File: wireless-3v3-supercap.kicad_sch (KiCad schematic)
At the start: 3 parts, among them J1 POWER-OUT, J2 POWER-IN

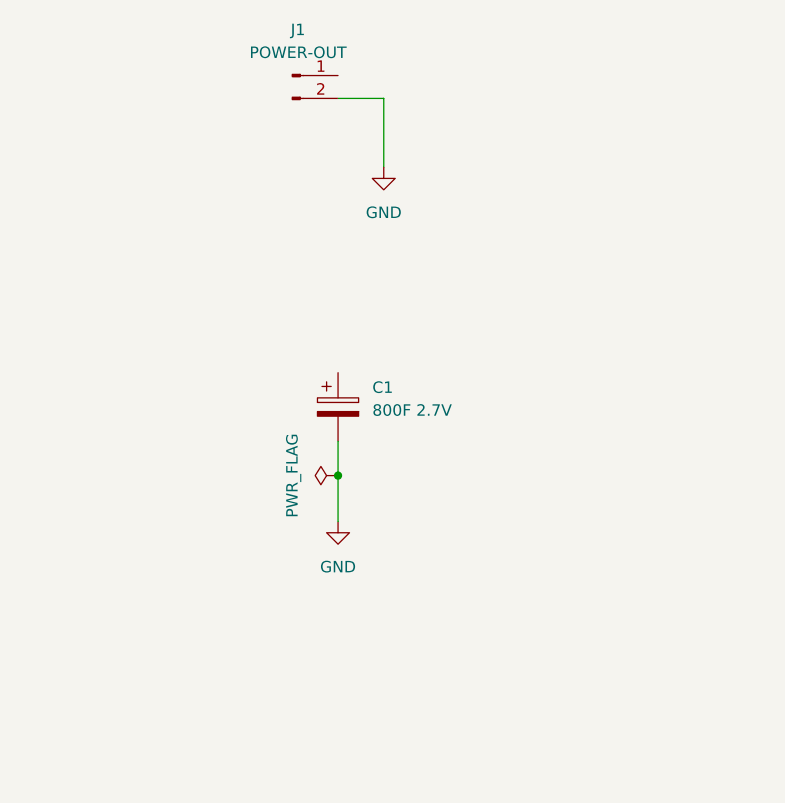
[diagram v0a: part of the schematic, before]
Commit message: Add a discharge switch
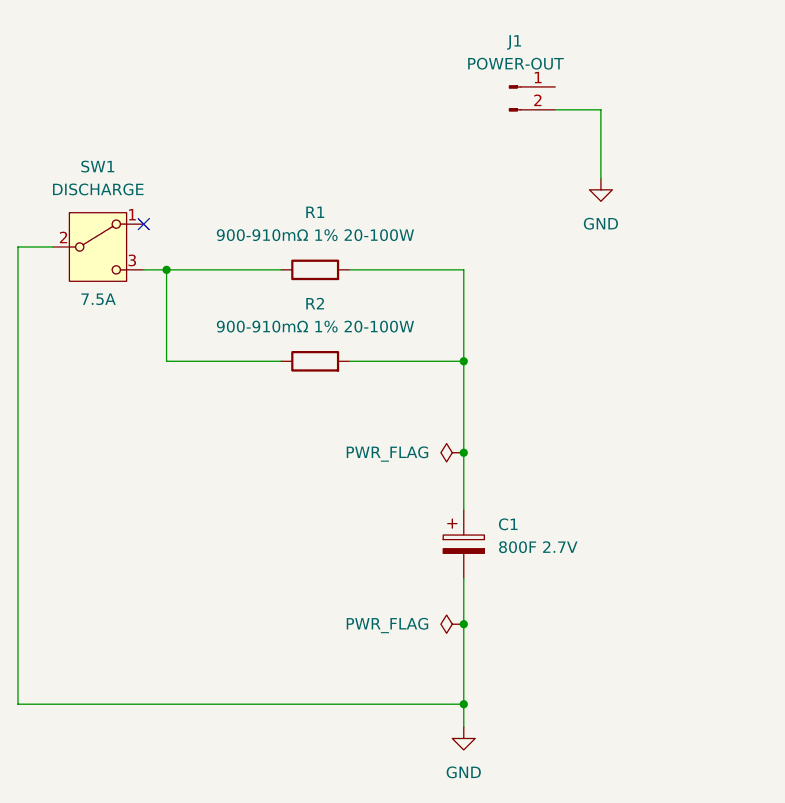
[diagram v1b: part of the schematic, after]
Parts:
- added R1, R2: 900-910mΩ 1% 20-100W, Package_TO_SOT_THT:TO-247-2_Horizontal_TabDown, symbol Device:R
- added SW1: DISCHARGE, symbol Switch:SW_SPDT
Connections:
- net GND: now also SW1.2 (B)
- net at C1.1: now also R1.2, R2.2
- new net: R1.1, R2.1, SW1.3 (C)
- no-connect marks 0 -> 1
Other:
- moved on the sheet: C1, J1

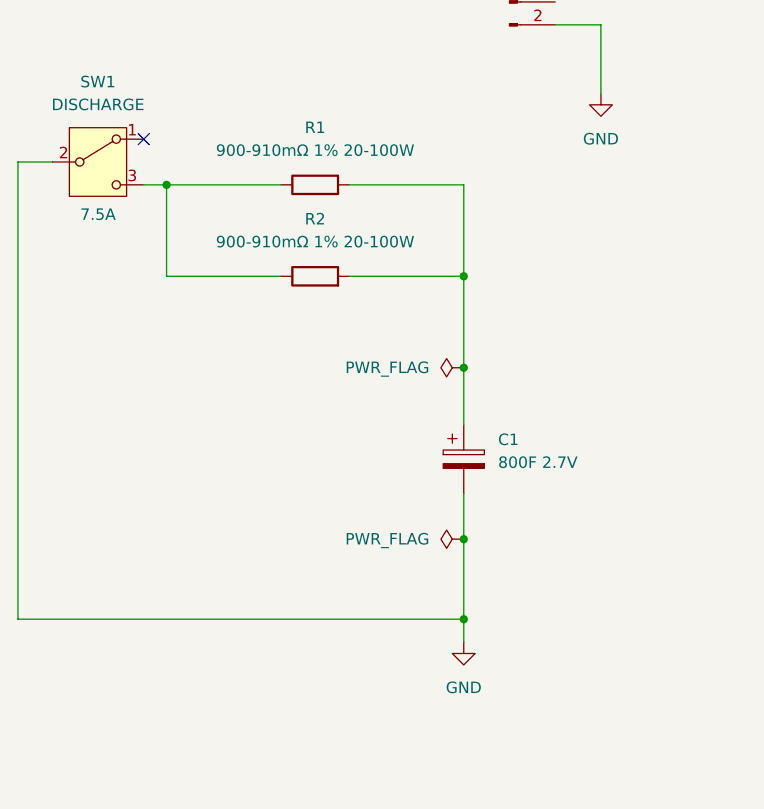
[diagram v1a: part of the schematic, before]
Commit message: Add heatsinks to the discharge resistors
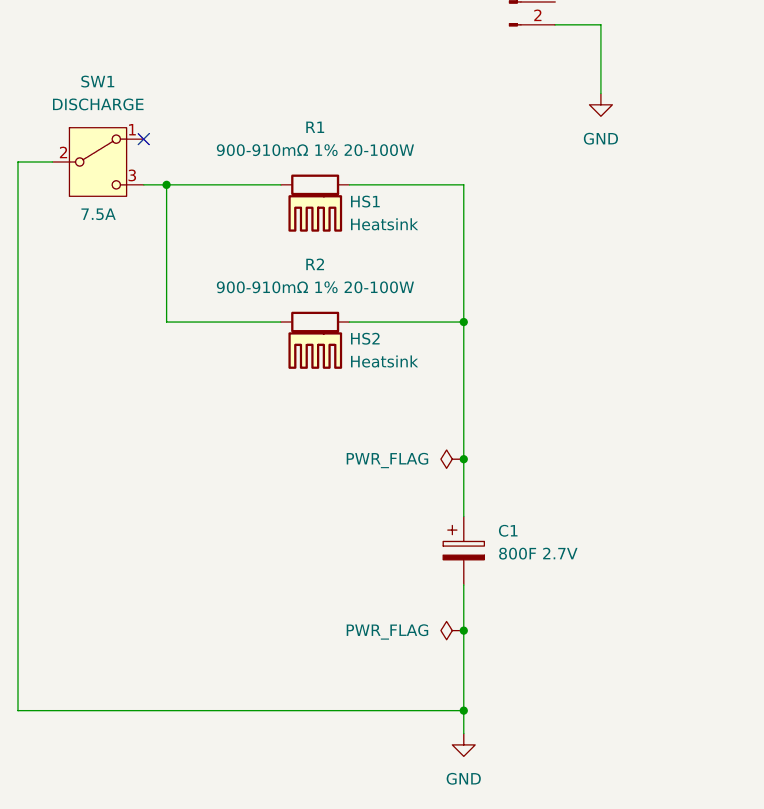
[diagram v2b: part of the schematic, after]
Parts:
- added HS1, HS2: Heatsink, symbol Mechanical:Heatsink
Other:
- moved on the sheet: C1, R2

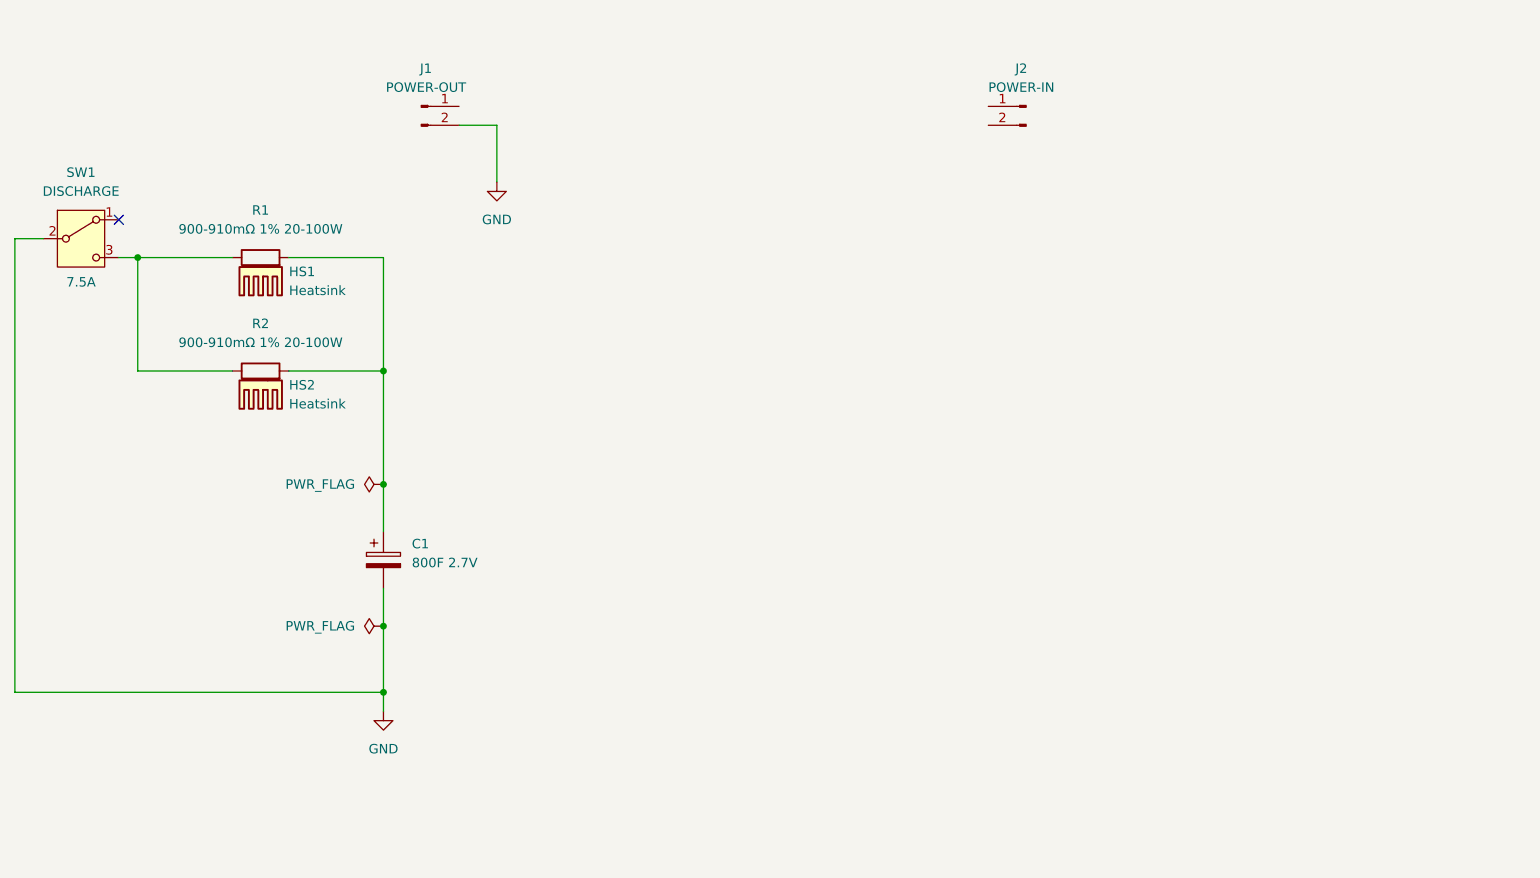
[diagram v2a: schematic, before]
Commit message: Add BQ33100PWR
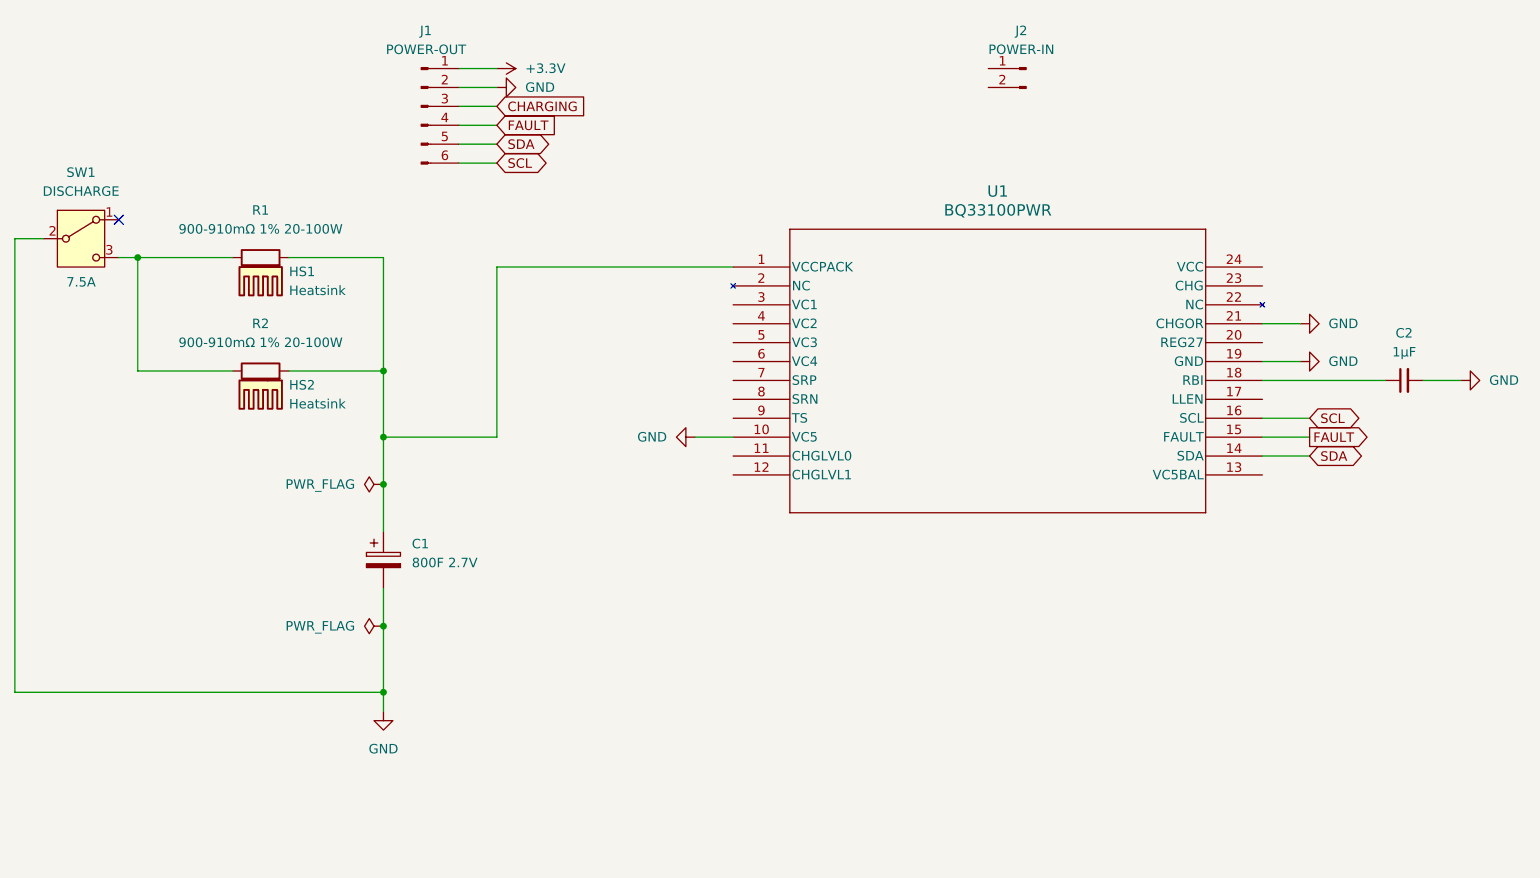
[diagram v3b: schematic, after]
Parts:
- added C2: 1µF, symbol Device:C_Small
- added U1: BQ33100PWR, PW24, symbol BQ33100PWR:BQ33100PWR
- J1: footprint Connector_PinHeader_2.54mm:PinHeader_1x02_P2.54mm_Vertical -> Connector_PinHeader_2.54mm:PinHeader_1x06_P2.54mm_Vertical; symbol Connector:Conn_01x02_Pin -> Connector:Conn_01x06_Pin
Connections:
- net GND: now also C2.2, U1.10 (VC5), U1.19 (GND), U1.21 (CHGOR)
- net +3.3V: now reaches J1.1 (Pin_1)
- net at C1.1, R1.2, R2.2: now also U1.1 (VCCPACK)
- new net: C2.1, U1.18 (RBI)
- new net CHARGING: J1.3 (Pin_3)
- new net FAULT: J1.4 (Pin_4), U1.15 (FAULT)
- new net SCL: J1.6 (Pin_6), U1.16 (SCL)
- new net SDA: J1.5 (Pin_5), U1.14 (SDA)
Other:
- moved on the sheet: J2

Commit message: Remove BQ33100PWR and discharge resistors
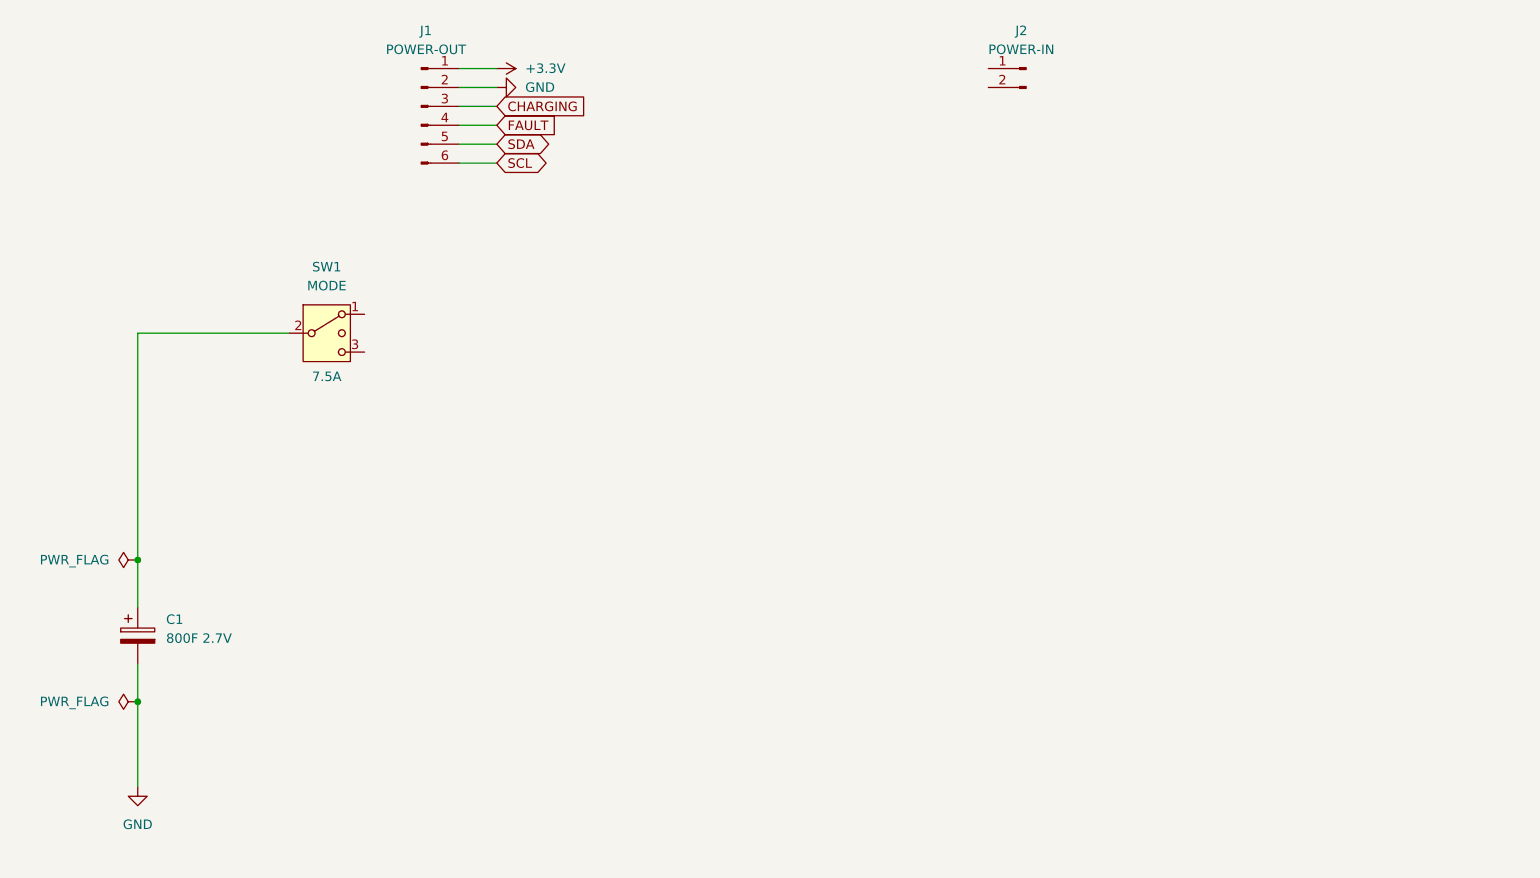
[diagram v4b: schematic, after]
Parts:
- removed C2: 1µF, symbol Device:C_Small
- removed HS1, HS2: Heatsink, symbol Mechanical:Heatsink
- removed R1, R2: 900-910mΩ 1% 20-100W, Package_TO_SOT_THT:TO-247-2_Horizontal_TabDown, symbol Device:R
- removed U1: BQ33100PWR, PW24, symbol BQ33100PWR:BQ33100PWR
- SW1: value DISCHARGE -> MODE; symbol Switch:SW_SPDT -> Switch:SW_SPDT_MSM
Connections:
- net GND: no longer SW1.2 (B)
- net at C1.1: now also SW1.2 (3)
- no-connect marks 1 -> 0
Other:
- moved on the sheet: C1

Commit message: Add discharge circuit, and main component for charging/power out
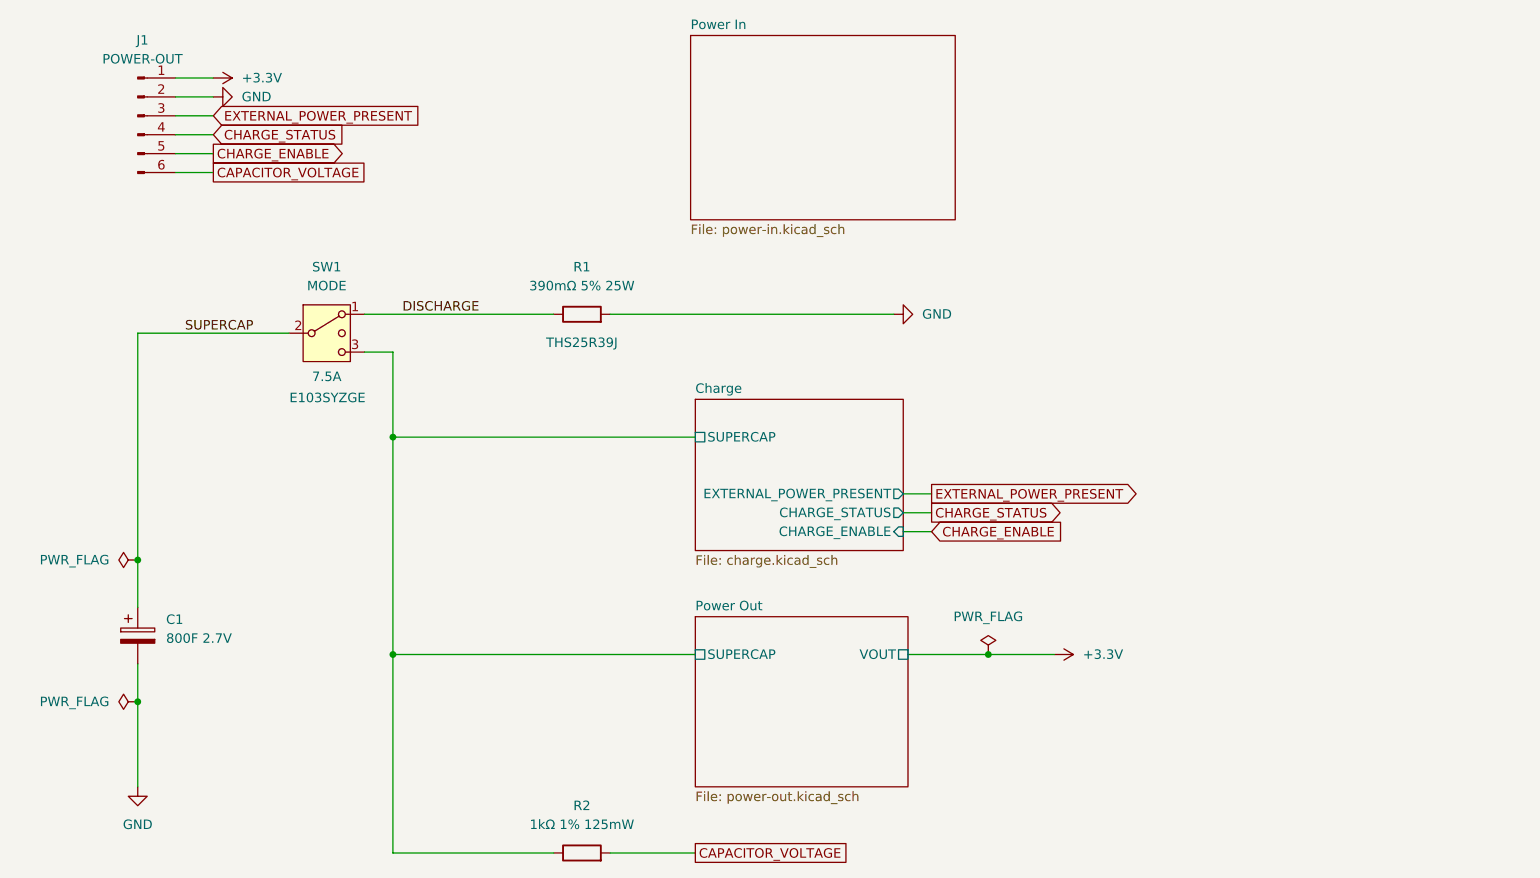
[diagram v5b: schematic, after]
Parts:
- removed J2: POWER-IN, Connector_PinHeader_2.54mm:PinHeader_1x02_P2.54mm_Vertical, symbol Connector:Conn_01x02_Pin
- added R1: 390mΩ 5% 25W, wireless-3v3-supercap:THS25R39J, symbol Device:R
- added R2: 1kΩ 1% 125mW, symbol Device:R
- SW1: footprint (none) -> wireless-3v3-supercap:E103SYZGE; Part Number (none) -> E103SYZGE
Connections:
- net GND: now also R1.2
- net DISCHARGE: now reaches SW1.1
- net DISCHARGE: now also R1.1
- net SUPERCAP: now reaches C1.1, SW1.2 (3)
- net Charge/SUPERCAP: now reaches SW1.3 (4)
- net Charge/SUPERCAP: now also R2.1
- net CHARGING renamed EXTERNAL_POWER_PRESENT
- net FAULT renamed CHARGE_STATUS
- net SCL renamed CAPACITOR_VOLTAGE
- net CAPACITOR_VOLTAGE: now also R2.2
- net SDA renamed CHARGE_ENABLE
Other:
- added sheet Charge (charge.kicad_sch)
- added sheet Power In (power-in.kicad_sch)
- added sheet Power Out (power-out.kicad_sch)
- moved on the sheet: J1

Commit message: Add power output capacitors
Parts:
- R2: footprint (none) -> Resistor_SMD:R_0805_2012Metric_Pad1.20x1.40mm_HandSolder
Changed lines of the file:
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@@
 			)
 		)
-		(property "Footprint" ""
+		(property "Footprint" "Resistor_SMD:R_0805_2012Metric_Pad1.20x1.40mm_HandSolder"
 			(at 85.09 121.158 90)
 			(effects
